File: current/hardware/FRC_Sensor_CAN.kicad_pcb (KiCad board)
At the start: 4 copper layers, 52 x 74 mm, 144 parts, among them J1 2P PUSH 3.5mm, J2 2P PUSH 3.5mm, J3 2P PUSH 3.5mm, J4 3P PUSH 3.5mm, J5 3P PUSH 3.5mm, J6 3P PUSH 3.5mm, J8 2x5 SERVICE SOCKET 2.54mm, Q1 AO4485, Q101 AO3401A, Q102 BSS138BK, Q2 BSS138BK, Q201 AO3401A, Q202 BSS138BK, Q3 BSS138BK, Q301 AO3401A, Q302 BSS138BK, U1 LMR51420XDDCR, U10 SN74AHCT1G125, U2 AP2112K-3.3, U4 TPS2553DBVR-1, U5 STM32F042K6T6, U6 TCAN3413DR, U7 LM339LV, U8 TPS61085DGKR, U9 TPS259620DDAR, Y1 8MHz 18pF

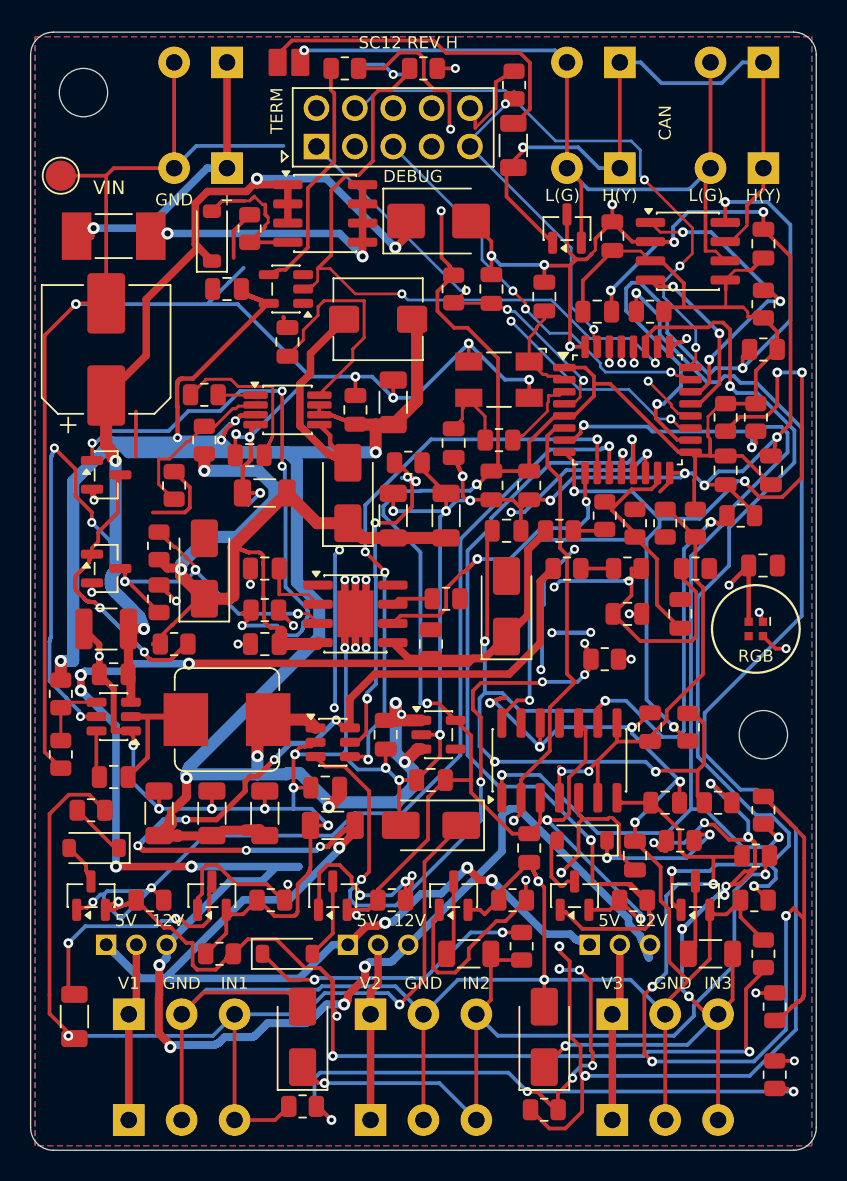
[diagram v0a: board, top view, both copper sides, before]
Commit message: Enforce straight routing and remove redundant PCB traces
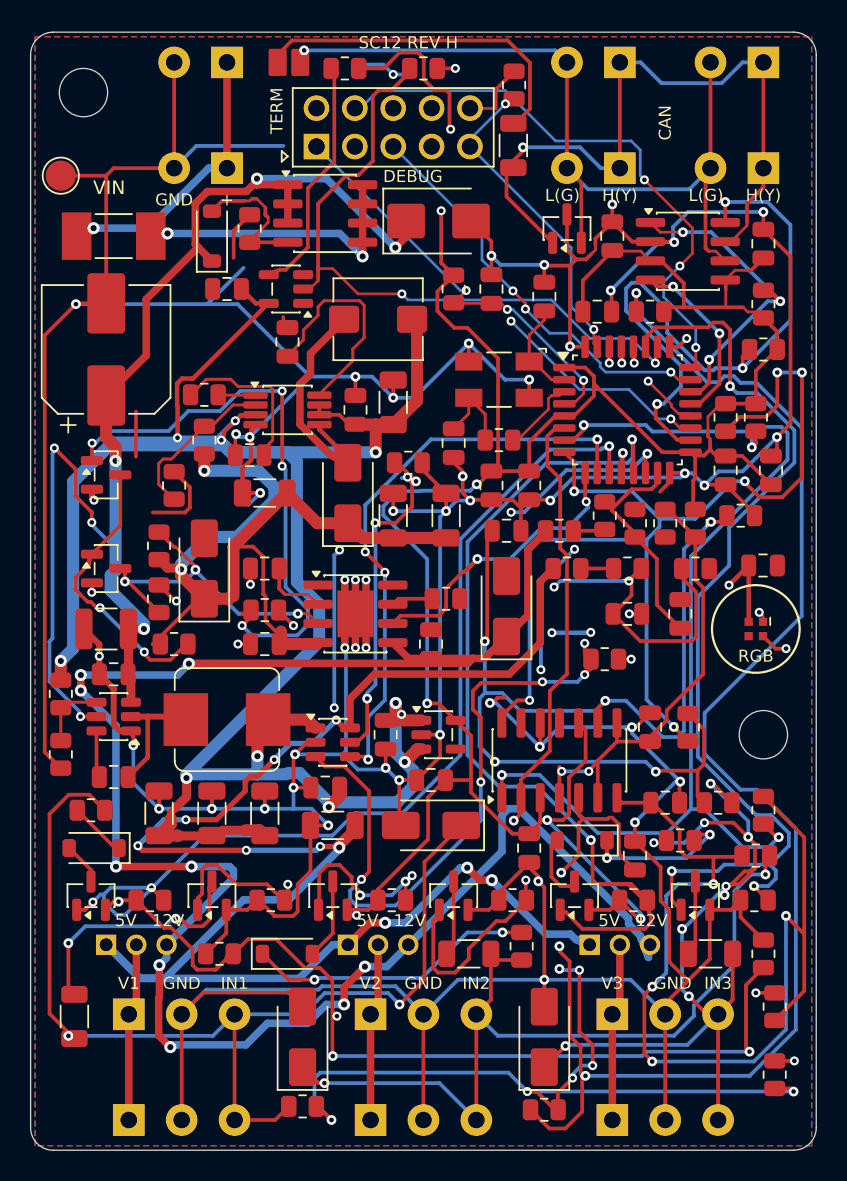
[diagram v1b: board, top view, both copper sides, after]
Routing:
- net SENSOR_12V: track 160.7 -> 123.8 mm
- net V5_INTERNAL: track 207.8 -> 191.8 mm
- net EFUSE_INHIBIT: track 31.5 -> 18.5 mm
- net SENSE2: track 71.4 -> 63.4 mm
- net SIG3: track 64.4 -> 58.2 mm
- net VIN_PROT: track 96.3 -> 90.1 mm
- net +3V3: track 245.4 -> 239.4 mm
- net GND: track 502.6 -> 496.6 mm
- net BIAS_UP2_N: track 50.0 -> 48.4 mm
- net VPORT2: track 13.3 -> 11.8 mm
- net SENSOR_5V: track 114.6 -> 113.2 mm
- net BOOST_12V: track 58.5 -> 57.4 mm
- net BUCK_SW: track 9.37 -> 8.26 mm
- net BOOT0: track 22.1 -> 21.3 mm
- net BOOST_SW: track 15.8 -> 15.1 mm
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
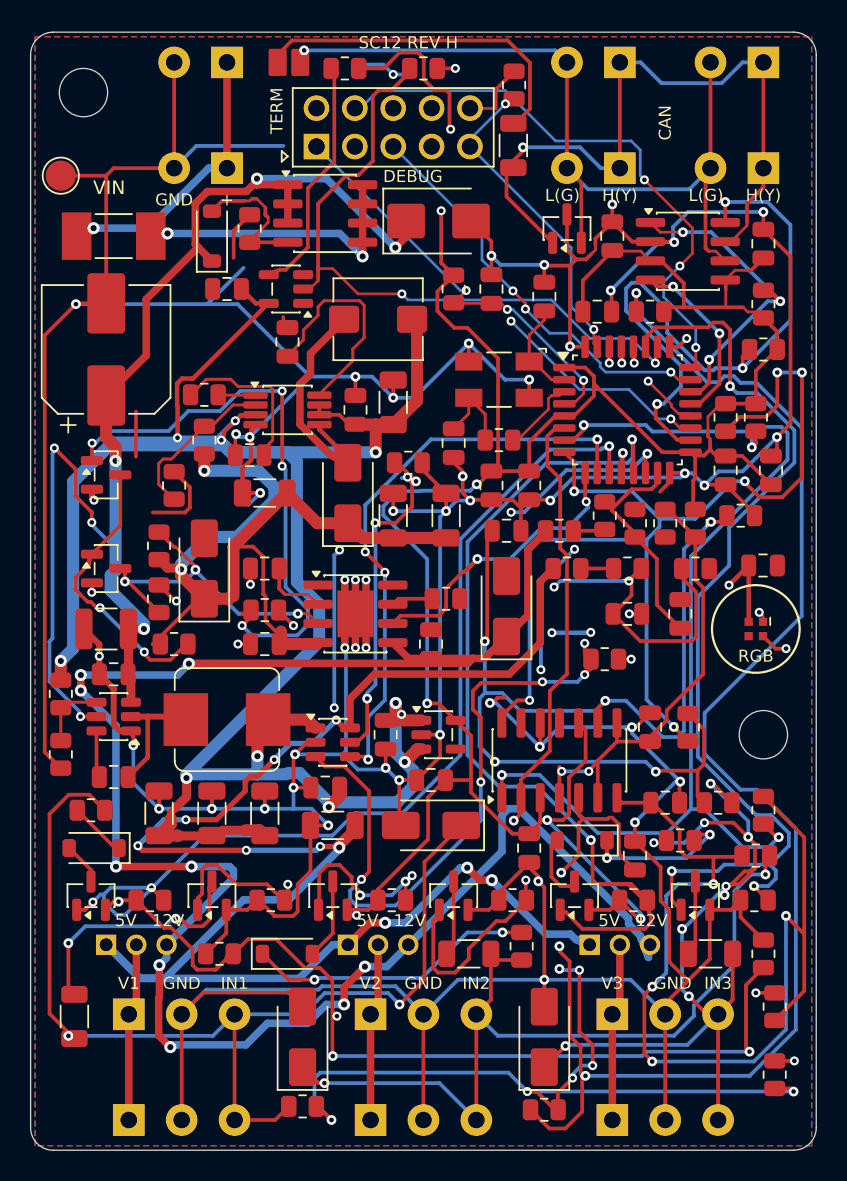
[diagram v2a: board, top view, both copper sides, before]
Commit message: Clean routing junctions and enforce explicit chamfered branches
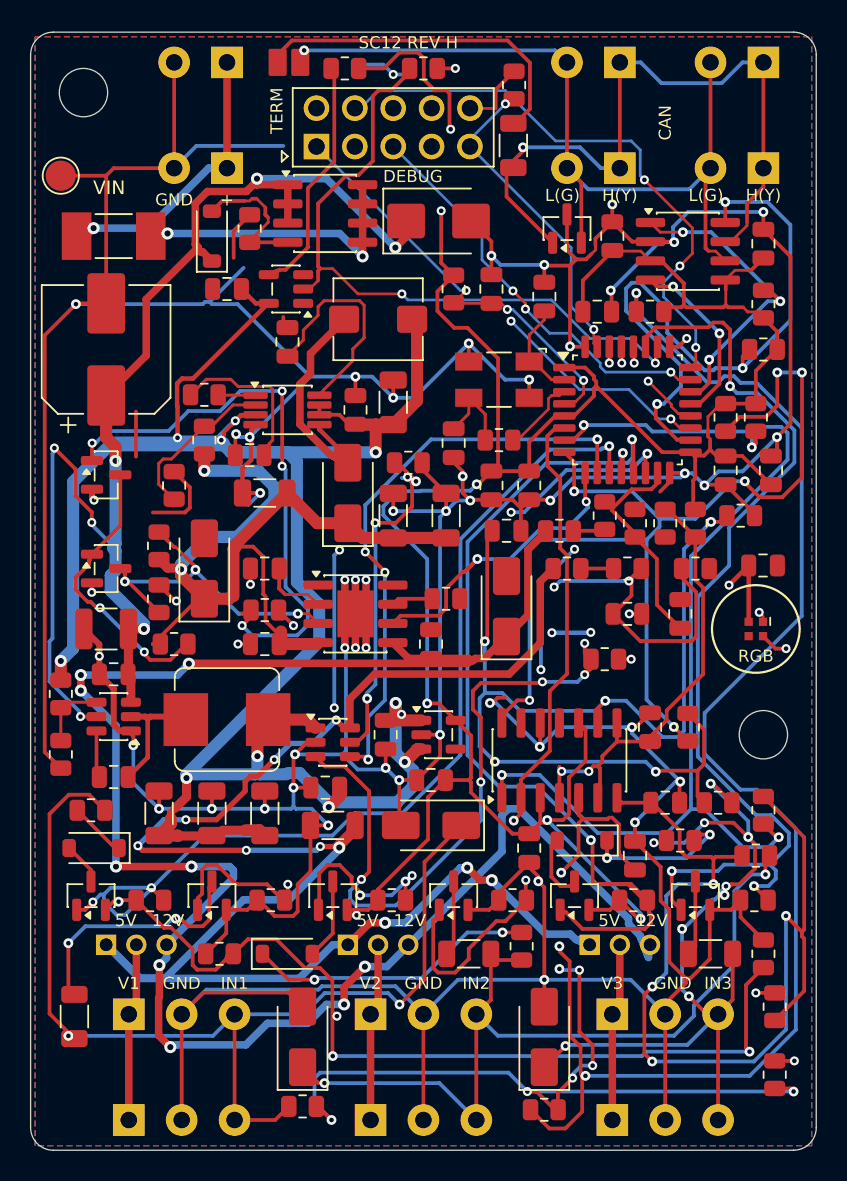
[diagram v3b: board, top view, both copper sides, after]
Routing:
- net V5_INTERNAL: track 191.8 -> 180.7 mm
- net SIG3: track 58.2 -> 56.0 mm
